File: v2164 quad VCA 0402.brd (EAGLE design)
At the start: 39.4 x 14.6 mm, 43 parts, among them IC1 TL072JD, IC2 TL072JD

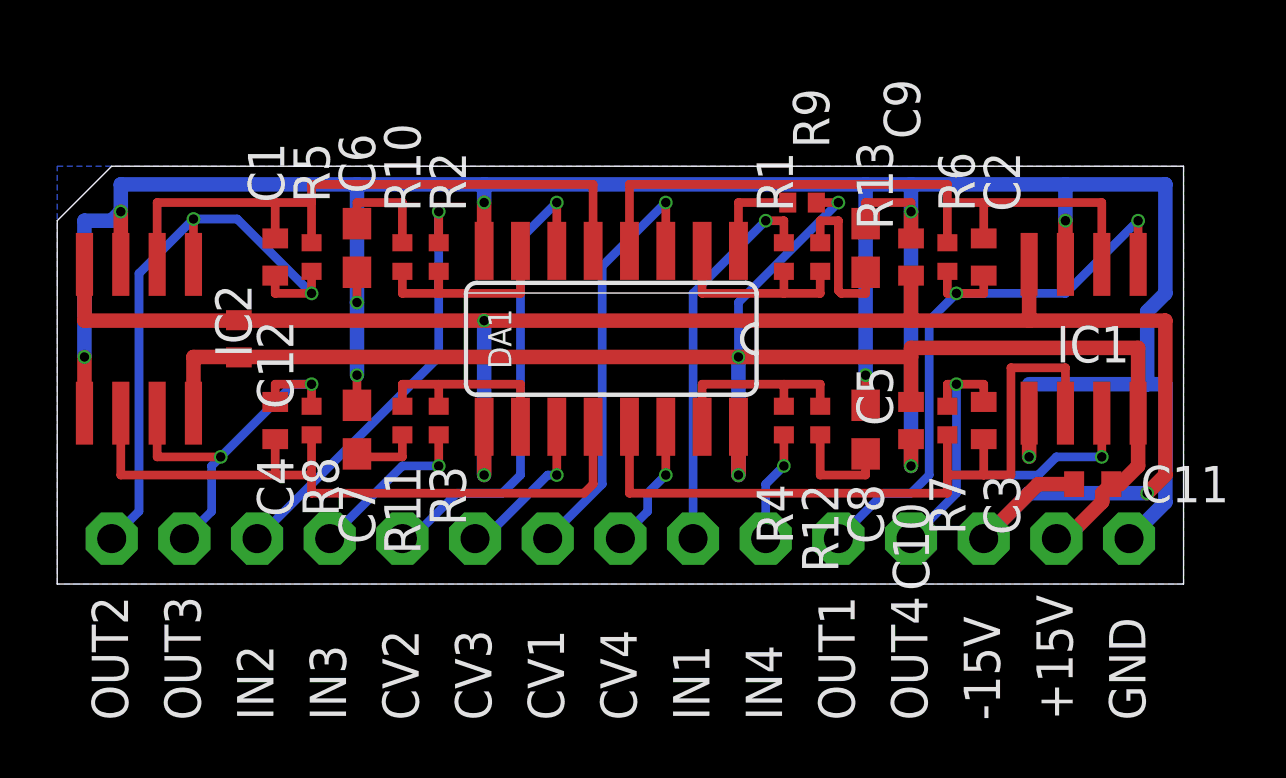
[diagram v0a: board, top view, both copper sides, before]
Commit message: Finished top layer on both boards i think
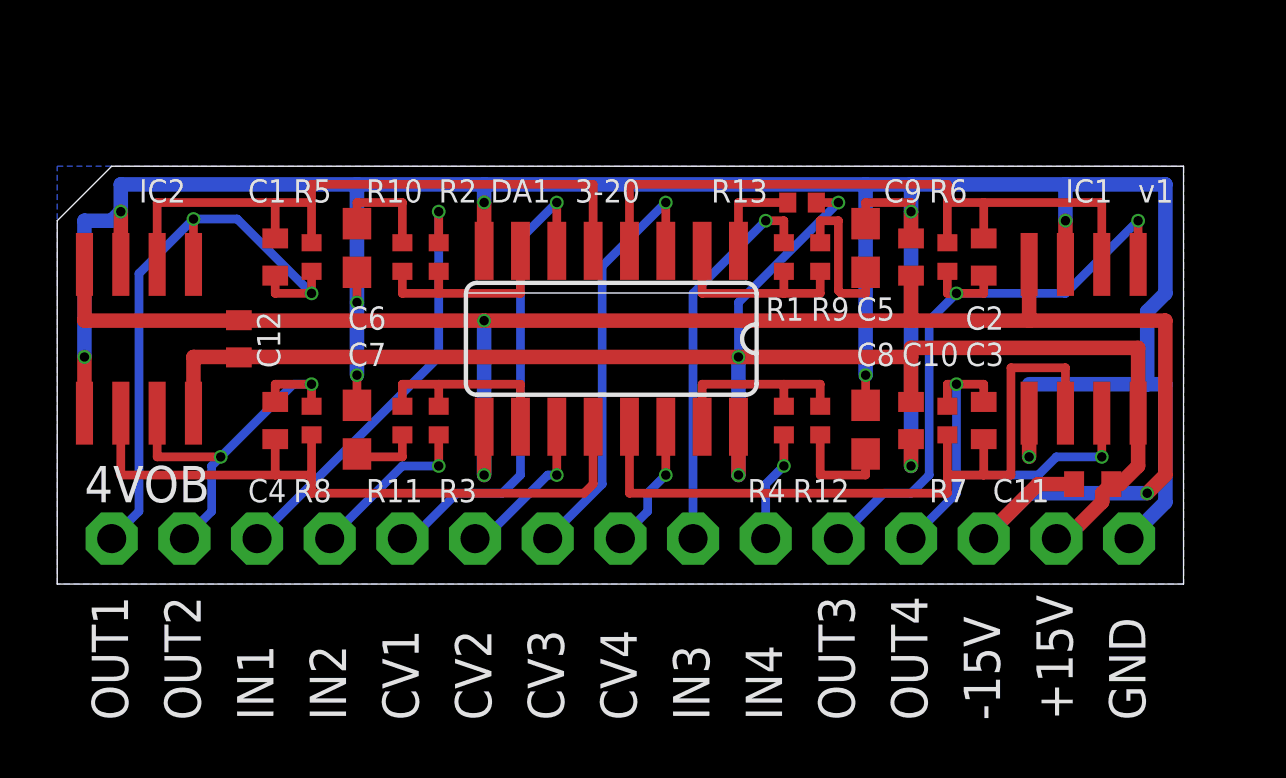
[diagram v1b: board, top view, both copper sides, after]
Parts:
- moved OUT1 25.4 mm to (1.91, 1.59)
- moved OUT3 22.9 mm to (27.3, 1.59)
- moved IN1 15.2 mm to (6.99, 1.59)
- moved IN3 12.7 mm to (22.2, 1.59)
- moved CV1 5.08 mm to (12.1, 1.59)
- moved CV2 2.54 mm to (14.6, 1.59)
- moved IN2 2.54 mm to (9.53, 1.59)
- moved OUT2 2.54 mm to (4.45, 1.59)
- moved CV3 2.54 mm to (17.1, 1.59)
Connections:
- net CV1: now also DA1.6; no longer DA1.3
- net CV2: now also DA1.11; no longer DA1.6
- net CV3: now also DA1.3; no longer DA1.11
- net IN1: now also R2.1; no longer R1.1
- net IN2: now also R3.1; no longer R2.1
- net IN3: now also R1.1; no longer R3.1
- net OUT1: now also C1.2, IC2.1, R5.2; no longer C2.2, IC1.1, R6.2
- net OUT2: now also C4.2, IC2.7, R8.2; no longer C1.2, IC2.1, R5.2
- net OUT3: now also C2.2, IC1.1, R6.2; no longer C4.2, IC2.7, R8.2
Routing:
- net CV2: track 16.8 -> 5.47 mm
- net CV3: track 5.47 -> 15.1 mm
- net IN2: track 15.1 -> 5.95 mm
- net OUT3: track 14.0 -> 22.4 mm
- net OUT2: track 21.8 -> 14.0 mm
- net IN3: track 5.95 -> 13.6 mm
- net CV1: track 15.1 -> 16.8 mm
- net IN1: track 13.6 -> 15.1 mm
- net OUT1: track 22.4 -> 21.8 mm
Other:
- board text added: "3-20"
- board text added: "4VOB"
- board text added: "v1"

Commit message: Completed silkscreen and routing on both vca and mixer.
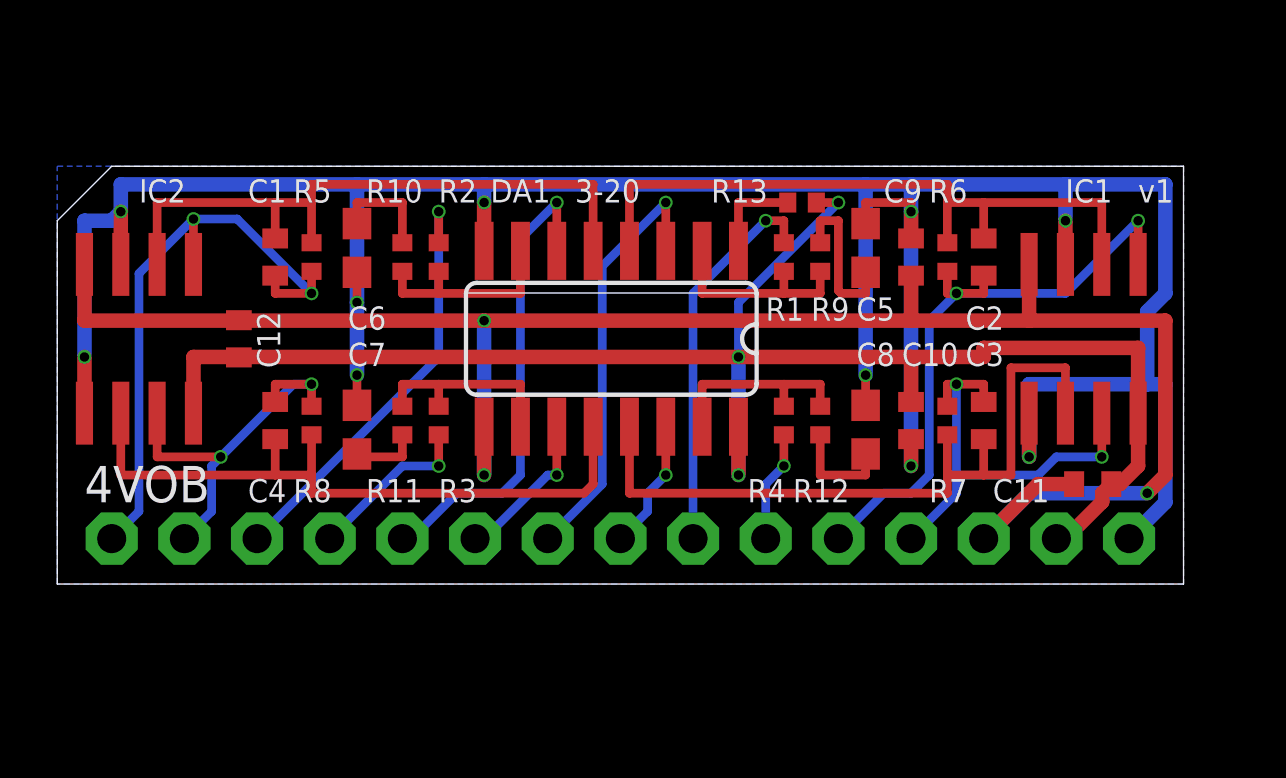
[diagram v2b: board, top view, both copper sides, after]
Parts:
- added U$1: (no value), joakim:XONIK_LOGO_20
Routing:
- net GND: track 102.9 -> 105.4 mm
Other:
- board text added: "+15v"
- board text added: "-15v"
- board text added: "AGND"
- board text added: "C1"
- board text added: "C2"
- board text added: "C3"
- board text added: "C4"
- board text added: "I1"
- board text added: "I2"
- board text added: "I3"
- board text added: "I4"
- board text added: "O1"
- board text added: "O2"
- board text added: "O3"
- board text added: "O4"
- board text added: "Quad exp VCA"
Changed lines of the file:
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@@
 <text x="37.7825" y="13.335" size="0.8128" layer="25" font="vector">v1</text>
 <text x="18.0975" y="13.335" size="0.8128" layer="25" font="vector">3-20</text>
+<text x="1.27" y="3.175" size="1.27" layer="26" font="vector" rot="MR90">O1</text>
+<text x="3.81" y="3.175" size="1.27" layer="26" font="vector" rot="MR90">O2</text>
+<text x="6.35" y="3.175" size="1.27" layer="26" font="vector" rot="MR90">I1</text>
+<text x="8.89" y="3.175" size="1.27" layer="26" font="vector" rot="MR90">I2</text>
+<text x="11.43" y="3.175" size="1.27" layer="26" font="vector" rot="MR90">C1</text>
+<text x="13.97" y="3.175" size="1.27" layer="26" font="vector" rot="MR90">C2</text>
+<text x="16.51" y="3.175" size="1.27" layer="26" font="vector" rot="MR90">C3</text>
+<text x="19.05" y="3.175" size="1.27" layer="26" font="vector" rot="MR90">C4</text>
+<text x="21.59" y="3.175" size="1.27" layer="26" font="vector" rot="MR90">I3</text>
+<text x="24.13" y="3.175" size="1.27" layer="26" font="vector" rot="MR90">I4</text>
+<text x="26.67" y="3.175" size="1.27" layer="26" font="vector" rot="MR90">O3</text>
+<text x="29.21" y="3.175" size="1.27" layer="26" font="vector" rot="MR90">O4</text>
+<text x="34.29" y="3.175" size="1.27" layer="26" font="vector" rot="MR90">+15v</text>
+<text x="31.75" y="3.175" size="1.27" layer="26" font="vector" rot="MR90">-15v</text>
+<text x="36.83" y="3.175" size="1.27" layer="26" font="vector" rot="MR90">AGND</text>
+<text x="25.4" y="6.0325" size="1.27" layer="26" font="vector" rot="MR0">Quad exp VCA</text>
 </plain>
 <attributes>
@@
 </element>
 <element name="CV3" library="joakim" package="MA01N-1J" value="" x="17.145" y="1.5875" smashed="yes" rot="R90">
-<attribute name="NAME" x="17.7165" y="-4.7625" size="1.27" layer="25" ratio="10" rot="R90"/>
 <attribute name="VALUE" x="20.066" y="-0.9525" size="1.27" layer="27" ratio="10" rot="R90"/>
 </element>
 <element name="CV1" library="joakim" package="MA01N-1J" value="" x="12.065" y="1.5875" smashed="yes" rot="R90">
-<attribute name="NAME" x="12.6365" y="-4.7625" size="1.27" layer="25" ratio="10" rot="R90"/>
 <attribute name="VALUE" x="14.986" y="-0.9525" size="1.27" layer="27" ratio="10" rot="R90"/>
 </element>
 <element name="CV2" library="joakim" package="MA01N-1J" value="" x="14.605" y="1.5875" smashed="yes" rot="R90">
-<attribute name="NAME" x="15.1765" y="-4.7625" size="1.27" layer="25" ratio="10" rot="R90"/>
 <attribute name="VALUE" x="17.526" y="-0.9525" size="1.27" layer="27" ratio="10" rot="R90"/>
 </element>
 <element name="CV4" library="joakim" package="MA01N-1J" value="" x="19.685" y="1.5875" smashed="yes" rot="R90">
-<attribute name="NAME" x="20.2565" y="-4.7625" size="1.27" layer="25" ratio="10" rot="R90"/>
 <attribute name="VALUE" x="22.606" y="-0.9525" size="1.27" layer="27" ratio="10" rot="R90"/>
 </element>
 <element name="IN3" library="joakim" package="MA01N-1J" value="" x="22.225" y="1.5875" smashed="yes" rot="R90">
-<attribute name="NAME" x="22.7965" y="-4.7625" size="1.27" layer="25" ratio="10" rot="R90"/>
 <attribute name="VALUE" x="25.146" y="-0.9525" size="1.27" layer="27" ratio="10" rot="R90"/>
 </element>
 <element name="IN1" library="joakim" package="MA01N-1J" value="" x="6.985" y="1.5875" smashed="yes" rot="R90">
-<attribute name="NAME" x="7.5565" y="-4.7625" size="1.27" layer="25" ratio="10" rot="R90"/>
 <attribute name="VALUE" x="9.906" y="-0.9525" size="1.27" layer="27" ratio="10" rot="R90"/>
 </element>
 <element name="IN2" library="joakim" package="MA01N-1J" value="" x="9.525" y="1.5875" smashed="yes" rot="R90">
-<attribute name="NAME" x="10.0965" y="-4.7625" size="1.27" layer="25" ratio="10" rot="R90"/>
 <attribute name="VALUE" x="12.446" y="-0.9525" size="1.27" layer="27" ratio="10" rot="R90"/>
 </element>
 <element name="IN4" library="joakim" package="MA01N-1J" value="" x="24.765" y="1.5875" smashed="yes" rot="R90">
-<attribute name="NAME" x="25.3365" y="-4.7625" size="1.27" layer="25" ratio="10" rot="R90"/>
 <attribute name="VALUE" x="27.686" y="-0.9525" size="1.27" layer="27" ratio="10" rot="R90"/>
 </element>
 <element name="OUT1" library="joakim" package="MA01N-1J" value="" x="1.905" y="1.5875" smashed="yes" rot="R90">
-<attribute name="NAME" x="2.4765" y="-4.7625" size="1.27" layer="25" ratio="10" rot="R90"/>
 <attribute name="VALUE" x="4.826" y="-0.9525" size="1.27" layer="27" ratio="10" rot="R90"/>
 </element>
 <element name="OUT3" library="joakim" package="MA01N-1J" value="" x="27.305" y="1.5875" smashed="yes" rot="R90">
-<attribute name="NAME" x="27.8765" y="-4.7625" size="1.27" layer="25" ratio="10" rot="R90"/>
 <attribute name="VALUE" x="30.226" y="-0.9525" size="1.27" layer="27" ratio="10" rot="R90"/>
 </element>
 <element name="OUT4" library="joakim" package="MA01N-1J" value="" x="29.845" y="1.5875" smashed="yes" rot="R90">
-<attribute name="NAME" x="30.4165" y="-4.7625" size="1.27" layer="25" ratio="10" rot="R90"/>
 <attribute name="VALUE" x="32.766" y="-0.9525" size="1.27" layer="27" ratio="10" rot="R90"/>
 </element>
 <element name="OUT2" library="joakim" package="MA01N-1J" value="" x="4.445" y="1.5875" smashed="yes" rot="R90">
-<attribute name="NAME" x="5.0165" y="-4.7625" size="1.27" layer="25" ratio="10" rot="R90"/>
 <attribute name="VALUE" x="7.366" y="-0.9525" size="1.27" layer="27" ratio="10" rot="R90"/>
 </element>
@@
 </element>
 <element name="+15V" library="joakim" package="MA01N-1J" value="" x="34.925" y="1.5875" smashed="yes" rot="R90">
-<attribute name="NAME" x="35.4965" y="-4.7625" size="1.27" layer="25" ratio="10" rot="R90"/>
 <attribute name="VALUE" x="37.846" y="-0.9525" size="1.27" layer="27" ratio="10" rot="R90"/>
 </element>
 <element name="GND" library="joakim" package="MA01N-1J" value="" x="37.465" y="1.5875" smashed="yes" rot="R90">
-<attribute name="NAME" x="38.0365" y="-4.7625" size="1.27" layer="25" ratio="10" rot="R90"/>
 <attribute name="VALUE" x="40.386" y="-0.9525" size="1.27" layer="27" ratio="10" rot="R90"/>
 </element>
 <element name="-15V" library="joakim" package="MA01N-1J" value="" x="32.385" y="1.5875" smashed="yes" rot="R90">
-<attribute name="NAME" x="32.9565" y="-4.7625" size="1.27" layer="25" ratio="10" rot="R90"/>
 <attribute name="VALUE" x="35.306" y="-0.9525" size="1.27" layer="27" ratio="10" rot="R90"/>
 </element>
@@
 <attribute name="VALUE" x="4.445" y="9.2075" size="1.27" layer="27" rot="R270"/>
 </element>
+<element name="U$1" library="joakim" package="XONIK_LOGO_20" value="" x="29.845" y="8.255" smashed="yes" rot="MR0"/>
 </elements>
 <signals>
@@
 <wire x1="33.9725" y1="5.9725" x2="33.9725" y2="4.445" width="0.508" layer="1"/>
 <via x="33.9725" y="4.445" extent="1-16" drill="0.3302"/>
-<wire x1="33.9725" y1="6.985" x2="38.1" y2="6.985" width="0.508" layer="16"/>
+<wire x1="38.1" y1="6.985" x2="33.9725" y2="6.985" width="0.508" layer="16"/>
 <wire x1="38.1" y1="9.525" x2="38.735" y2="10.16" width="0.508" layer="16"/>
 <wire x1="38.735" y1="10.16" x2="38.735" y2="13.97" width="0.508" layer="16"/>
@@
 <wire x1="38.735" y1="2.8575" x2="38.735" y2="6.985" width="0.508" layer="16"/>
 <wire x1="38.735" y1="6.985" x2="38.1" y2="6.985" width="0.508" layer="16"/>
+<wire x1="33.9725" y1="6.985" x2="33.9725" y2="4.445" width="0.508" layer="16"/>
 </signal>
 <signal name="N$1">
@@
 <contactref element="C12" pad="2"/>
 <wire x1="4.7625" y1="7.9375" x2="4.7625" y2="5.9725" width="0.508" layer="1"/>
-<wire x1="37.7825" y1="8.255" x2="29.845" y2="8.255" width="0.508" layer="1"/>
+<wire x1="37.7825" y1="8.255" x2="32.385" y2="8.255" width="0.508" layer="1"/>
+<wire x1="32.385" y1="7.9375" x2="29.845" y2="7.9375" width="0.508" layer="1"/>
 <wire x1="29.845" y1="7.9375" x2="23.8125" y2="7.9375" width="0.508" layer="1"/>
 <wire x1="23.8125" y1="7.9375" x2="6.35" y2="7.9375" width="0.508" layer="1"/>
@@
 <wire x1="6.35" y1="7.9225" x2="6.35" y2="7.9375" width="0.508" layer="1"/>
 <wire x1="29.845" y1="6.365" x2="29.845" y2="7.9375" width="0.508" layer="1"/>
-<wire x1="29.845" y1="7.9375" x2="29.845" y2="8.255" width="0.508" layer="1"/>
+<wire x1="32.385" y1="7.9375" x2="32.385" y2="8.255" width="0.508" layer="1"/>
 <wire x1="37.7825" y1="5.9725" x2="37.7825" y2="8.255" width="0.508" layer="1"/>
 <wire x1="23.8125" y1="5.4991" x2="23.8125" y2="3.81" width="0.508" layer="1"/>
